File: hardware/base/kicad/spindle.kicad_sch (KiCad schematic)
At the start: 29 parts, among them J16 SPINDLE, Q5 AO3422, Q6 AO3422, U31 LM2904DR2G, U32 SN74AHCT1G125DBVR

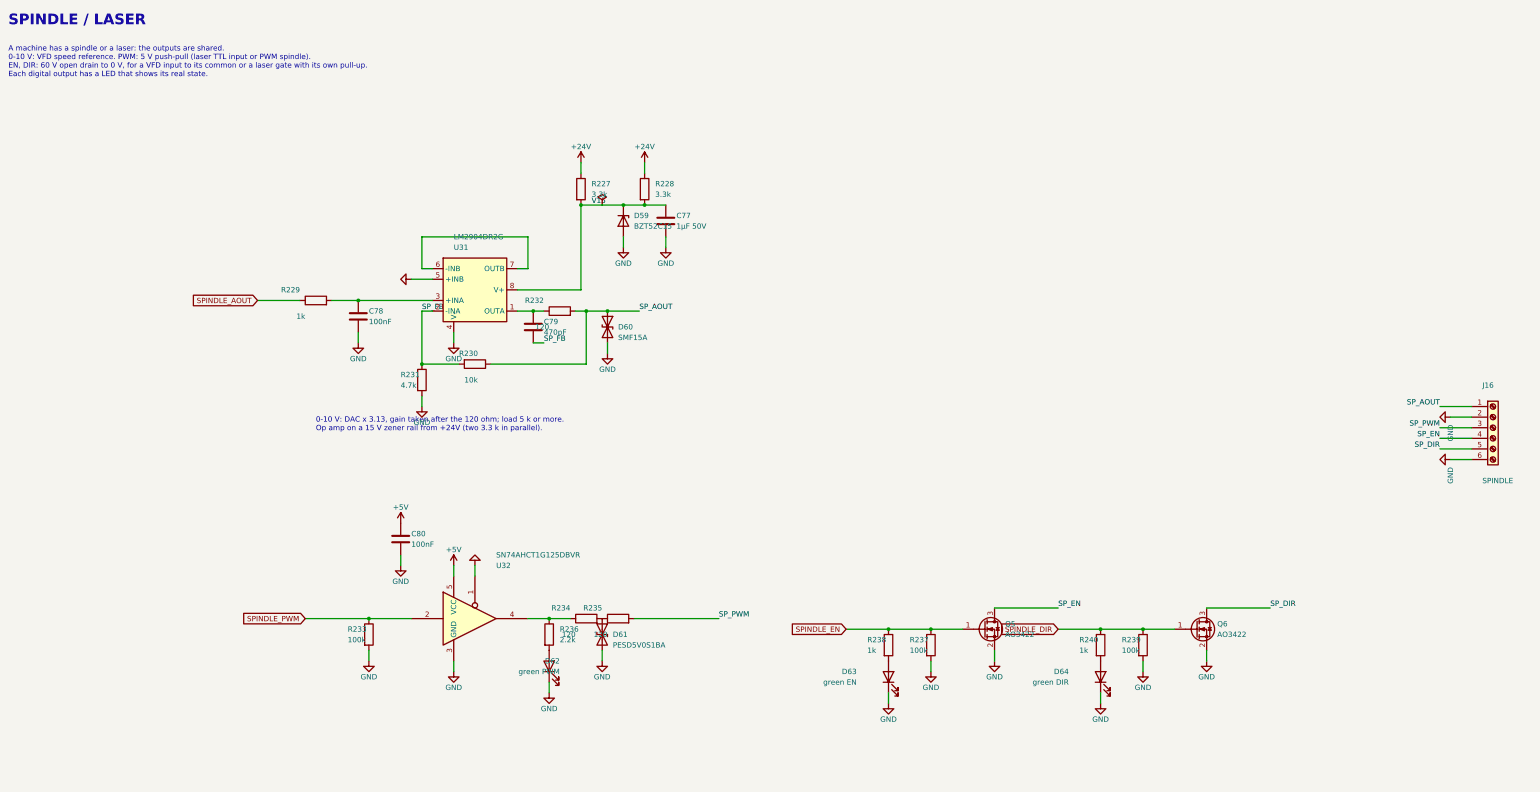
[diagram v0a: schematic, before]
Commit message: Harden the base board protections and unify its terminal blocks
- TVS (SMBJ33CA) on the spindle EN and DIR drains: a relay coil driven
  without a flyback diode no longer avalanches the FET.
- ESD (5 x TPD4E05U06) on every signal of the local bus header.
- A single terminal block type, KF2EDGR-3.81-4P, five times. Pinout rule:
  pole 1 withstands 24 V, pole 2 is 0 V, so the power plug damages
  nothing whichever header it lands in.
- Functional earth on pole 3 of the power terminal block, replacing the
  M3 earth lug.
- 100 k pull-down on the DAC node: the 0-10 V output stays at 0 V while
  the DAC pin is not configured (reset, bootloader).
- "24V OUT" LED on +24V_DRV and test points on the four rails.
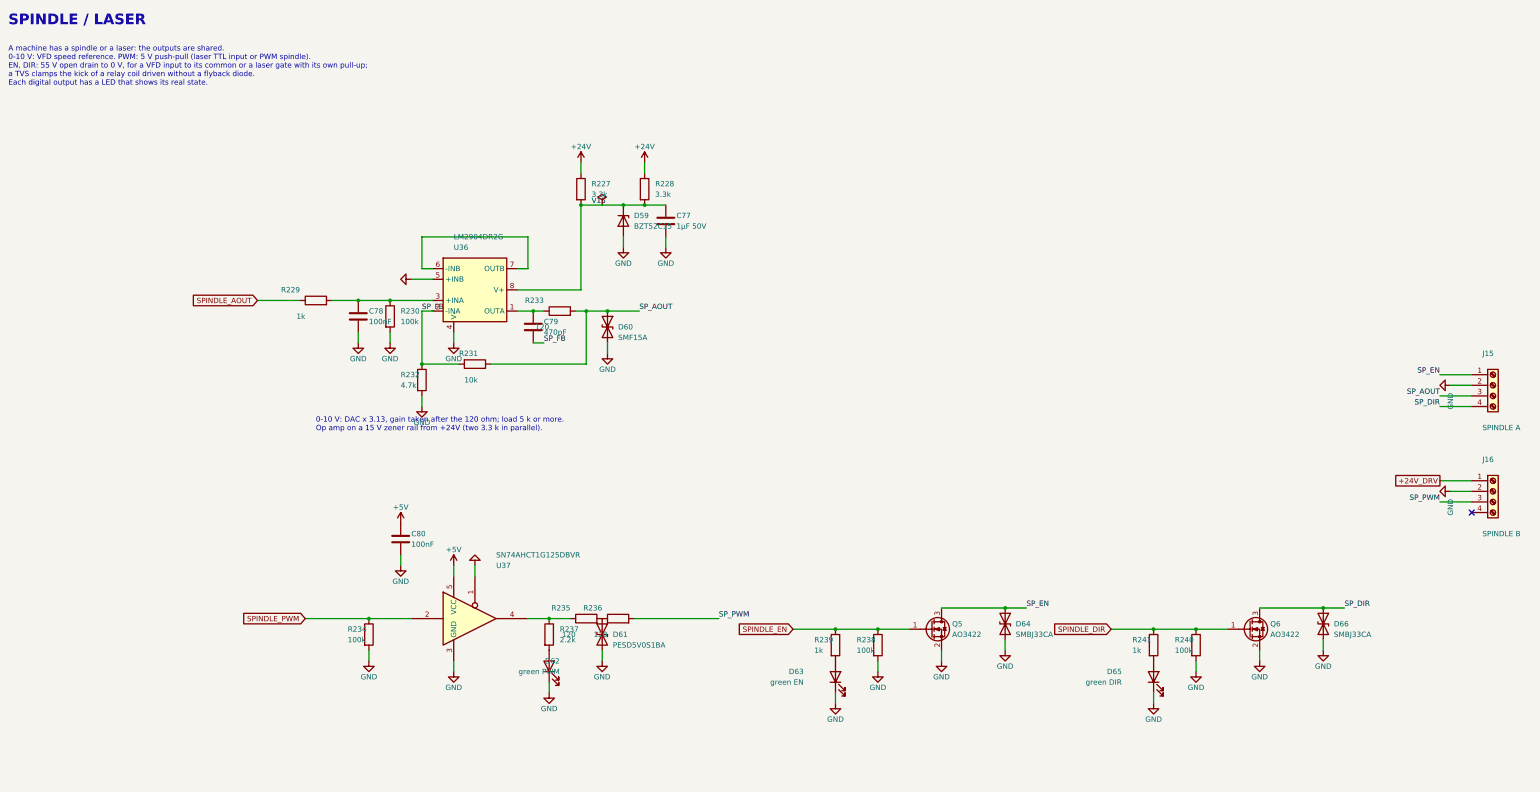
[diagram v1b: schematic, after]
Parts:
- removed U31: LM2904DR2G, Package_SO:SOIC-8_3.9x4.9mm_P1.27mm, symbol Bornier:OPAMP_DUAL
- removed U32: SN74AHCT1G125DBVR, Package_TO_SOT_SMD:SOT-23-5, symbol 74xGxx:74AHCT1G125
- added D65: green DIR, LED_SMD:LED_0603_1608Metric, symbol Device:LED
- added D66: SMBJ33CA, Diode_SMD:D_SMB, symbol Device:D_TVS
- added J15: SPINDLE A, Connector_Phoenix_MC:PhoenixContact_MC_1,5_4-G-3.81_1x04_P3.81mm_Horizontal, symbol Connector:Screw_Terminal_01x04
- added R241: 1k, Resistor_SMD:R_0402_1005Metric, symbol Device:R
- added U36: LM2904DR2G, Package_SO:SOIC-8_3.9x4.9mm_P1.27mm, symbol Bornier:OPAMP_DUAL
- added U37: SN74AHCT1G125DBVR, Package_TO_SOT_SMD:SOT-23-5, symbol 74xGxx:74AHCT1G125
- D64: value green DIR -> SMBJ33CA; footprint LED_SMD:LED_0603_1608Metric -> Diode_SMD:D_SMB; symbol Device:LED -> Device:D_TVS; LCSC C2289 -> C78420
- J16: value SPINDLE -> SPINDLE B; footprint Connector_Phoenix_MC:PhoenixContact_MC_1,5_6-G-3.81_1x06_P3.81mm_Horizontal -> Connector_Phoenix_MC:PhoenixContact_MC_1,5_4-G-3.81_1x04_P3.81mm_Horizontal; symbol Connector:Screw_Terminal_01x06 -> Connector:Screw_Terminal_01x04; LCSC C441186 -> C441184
- R230: value 10k -> 100k; LCSC C25744 -> C25741
- R231: value 4.7k -> 10k; LCSC C25900 -> C25744
- R232: value 120 -> 4.7k; footprint Resistor_SMD:R_0603_1608Metric -> Resistor_SMD:R_0402_1005Metric; LCSC C22787 -> C25900
- R233: value 100k -> 120; footprint Resistor_SMD:R_0402_1005Metric -> Resistor_SMD:R_0603_1608Metric; LCSC C25741 -> C22787
- R234: value 120 -> 100k; footprint Resistor_SMD:R_0603_1608Metric -> Resistor_SMD:R_0402_1005Metric; LCSC C22787 -> C25741
- R236: value 2.2k -> 120; footprint Resistor_SMD:R_0402_1005Metric -> Resistor_SMD:R_0603_1608Metric; LCSC C25879 -> C22787
- R237: value 100k -> 2.2k; LCSC C25741 -> C25879
- R238, R240: value 1k -> 100k; LCSC C11702 -> C25741
- R239: value 100k -> 1k; LCSC C25741 -> C11702
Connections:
- net +5V: now also U37.5 (VCC)
- net GND: now also D64.2 (A2), R230.2, R232.2, R234.2, R238.2, R240.2, D65.1 (K), D66.2 (A2), J15.2 (Pin_2), U36.4 (V-), U36.5 (+INB), U37.1, U37.3 (GND); no longer D64.1 (K), J16.6 (Pin_6), R231.2, R233.2, R237.2, R239.2
- net SPINDLE_DIR: now also R241.1; no longer R239.1
- net SPINDLE_EN: now also R239.1; no longer R237.1
- net SPINDLE_PWM: now also R234.1, U37.2; no longer R233.1
- net SP_AOUT: now also R231.1, R233.2, J15.3 (Pin_3); no longer J16.1 (Pin_1), R230.1, R232.2
- net SP_DIR: now also D66.1 (A1), J15.4 (Pin_4); no longer J16.5 (Pin_5)
- net SP_EN: now also D64.1 (A1), J15.1 (Pin_1); no longer J16.4 (Pin_4)
- net SP_FB: now also R231.2, R232.1, U36.2 (-INA); no longer R230.2, R231.1
- net SP_PWM: now also R236.2; no longer R235.2
- net V15: now also U36.8 (V+)
- net at D63.2 (A): now also R239.2; no longer R238.2
- net at C79.1: now also R233.1, U36.1 (OUTA); no longer R232.1
- net at R236.1: now also D61.1 (A1), R235.2; no longer R234.1
- net at D62.2 (A): now also R237.2; no longer R236.2
- net at C78.1, R229.2: now also R230.1, U36.3 (+INA)
- new net: D65.2 (A), R241.2
- new net: R235.1, R237.1, U37.4
- new net: U36.6 (-INB), U36.7 (OUTB)
- new net +24V_DRV: J16.1 (Pin_1)
- no-connect marks 0 -> 1
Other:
- note added: "A machine has a spindle or a laser: the outputs are shared. 0-10 V: VFD speed reference. PWM: 5 V push-pull (laser TTL input or PWM spindle). EN, DIR: 55 V open drain to 0 V, for a VFD input to its common or a laser gate with its own pull-up; a TVS clamps the kick of a relay coil driven without a flyback diode. Each digital output has a LED that shows its real state."
- note removed: "A machine has a spindle or a laser: the outputs are shared. 0-10 V: VFD speed reference. PWM: 5 V push-pull (laser TTL input or PWM spindle). EN, DIR: 60 V open drain to 0 V, for a VFD input to its common or a laser gate with its own pull-up. Each digital output has a LED that shows its real state."
- moved on the sheet: D63, Q5, Q6, R230, R231, R232, R233, R234, R235, R236, R237, R238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

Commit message: Accept a 12 V or 24 V supply on the base board (10.8 to 30 V)
- Supply nets renamed +VIN and +VIN_OUT (silkscreen VIN OUT).
- UVLO 200 k over 47 k // 100 k: start 8.47 V (9.48 V worst case),
  stop 7.79 V; fuse 3.5 A (12H1350C).
- 0-10 V: OPA2990 rail-to-rail op amp supplied by +VIN, SS8550 current
  limit across the 120 ohm; 10 V into 10 k from 10.9 V of supply.
- E-stop and probe inputs: 2 x 4.7 k in parallel, shunts 1 k and 4.7 k.
- Buck simulated from 7.8 to 30 V with the smallest slope compensation
  the datasheet allows: 79 deg, 11.6 dB minimum.
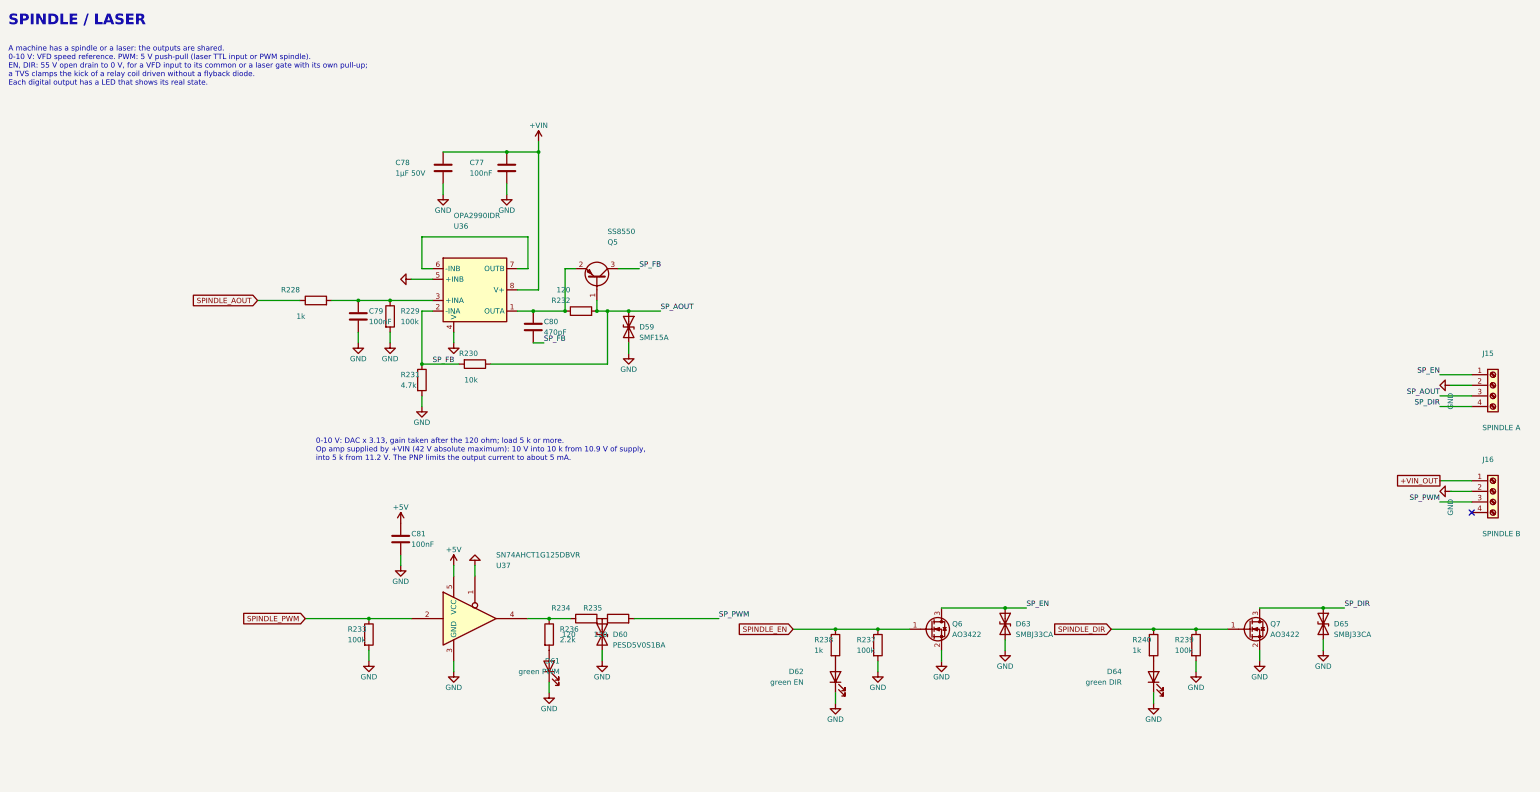
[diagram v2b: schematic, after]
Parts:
- removed D66: SMBJ33CA, Diode_SMD:D_SMB, symbol Device:D_TVS
- removed R227: 3.3k, Resistor_SMD:R_1206_3216Metric, symbol Device:R
- removed R241: 1k, Resistor_SMD:R_0402_1005Metric, symbol Device:R
- added C81: 100nF, Capacitor_SMD:C_0402_1005Metric, symbol Device:C
- added Q7: AO3422, Package_TO_SOT_SMD:SOT-23, symbol Transistor_FET:AO3400A
- C77: value 1µF 50V -> 100nF; footprint Capacitor_SMD:C_0603_1608Metric -> Capacitor_SMD:C_0402_1005Metric; LCSC C15849 -> C307331
- C78: value 100nF -> 1µF 50V; footprint Capacitor_SMD:C_0402_1005Metric -> Capacitor_SMD:C_0603_1608Metric; LCSC C307331 -> C15849
- C79: value 470pF -> 100nF; LCSC C1537 -> C307331
- C80: value 100nF -> 470pF; LCSC C307331 -> C1537
- D59: value BZT52C15 -> SMF15A; footprint Diode_SMD:D_SOD-123 -> Diode_SMD:D_SOD-123F; symbol Device:D_Zener -> Device:D_TVS; LCSC C2104 -> C123802
- D60: value SMF15A -> PESD5V0S1BA; footprint Diode_SMD:D_SOD-123F -> Diode_SMD:D_SOD-323; LCSC C123802 -> C19224
- D61: value PESD5V0S1BA -> green PWM; footprint Diode_SMD:D_SOD-323 -> LED_SMD:LED_0603_1608Metric; symbol Device:D_TVS -> Device:LED; LCSC C19224 -> C2289
- D62: value green PWM -> green EN
- D63: value green EN -> SMBJ33CA; footprint LED_SMD:LED_0603_1608Metric -> Diode_SMD:D_SMB; symbol Device:LED -> Device:D_TVS; LCSC C2289 -> C78420
- D64: value SMBJ33CA -> green DIR; footprint Diode_SMD:D_SMB -> LED_SMD:LED_0603_1608Metric; symbol Device:D_TVS -> Device:LED; LCSC C78420 -> C2289
- D65: value green DIR -> SMBJ33CA; footprint LED_SMD:LED_0603_1608Metric -> Diode_SMD:D_SMB; symbol Device:LED -> Device:D_TVS; LCSC C2289 -> C78420
- Q5: value AO3422 -> SS8550; symbol Transistor_FET:AO3400A -> Transistor_BJT:SS8550; LCSC C37130 -> C8542
- R228: value 3.3k -> 1k; footprint Resistor_SMD:R_1206_3216Metric -> Resistor_SMD:R_0402_1005Metric; LCSC C26032 -> C11702
- R229, R239: value 1k -> 100k; LCSC C11702 -> C25741
- R230: value 100k -> 10k; LCSC C25741 -> C25744
- R231: value 10k -> 4.7k; LCSC C25744 -> C25900
- R232: value 4.7k -> 120; footprint Resistor_SMD:R_0402_1005Metric -> Resistor_SMD:R_0603_1608Metric; LCSC C25900 -> C22787
- R233: value 120 -> 100k; footprint Resistor_SMD:R_0603_1608Metric -> Resistor_SMD:R_0402_1005Metric; LCSC C22787 -> C25741
- R234: value 100k -> 120; footprint Resistor_SMD:R_0402_1005Metric -> Resistor_SMD:R_0603_1608Metric; LCSC C25741 -> C22787
- R236: value 120 -> 2.2k; footprint Resistor_SMD:R_0603_1608Metric -> Resistor_SMD:R_0402_1005Metric; LCSC C22787 -> C25879
- R237: value 2.2k -> 100k; LCSC C25879 -> C25741
- R238, R240: value 100k -> 1k; LCSC C25741 -> C11702
- U36: value LM2904DR2G -> OPA2990IDR; LCSC C18229 -> C2058283
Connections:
- net +24V is gone; now on net SPINDLE_AOUT: R228.1
- net +5V: now also C81.1; no longer C80.1
- net GND: now also C79.2, D61.1 (K), D63.2 (A2), D64.1 (K), D65.2 (A2), R229.2, R231.2, R233.2, R237.2, R239.2, C81.2, Q7.2 (S); no longer C80.2, D61.2 (A2), D63.1 (K), D64.2 (A2), D65.1 (K), Q5.2 (S), R230.2, R232.2, R234.2, R238.2, R240.2
- net SPINDLE_AOUT: no longer R229.1
- net SPINDLE_DIR: now also R239.1, Q7.1 (G); no longer Q6.1 (G)
- net SPINDLE_EN: now also Q6.1 (G), R237.1; no longer Q5.1 (G), R239.1
- net SPINDLE_PWM: now also R233.1; no longer R234.1
- net SP_AOUT: now also D59.1 (A1), Q5.1 (B), R230.1, R232.2; no longer D60.1 (A1), R231.1, R233.2
- net SP_DIR: now also D65.1 (A1), Q7.3 (D); no longer Q6.3 (D)
- net SP_EN: now also D63.1 (A1), Q6.3 (D); no longer D64.1 (A1), Q5.3 (D)
- net SP_FB: now also C80.2, Q5.3 (C), R230.2, R231.1; no longer C79.2, R231.2, R232.1
- net SP_PWM: now also R235.2; no longer R236.2
- net at D62.2 (A): now also R238.2; no longer R237.2
- net +24V_DRV renamed +VIN_OUT
- net V15 renamed +VIN
- net +VIN: now also C78.1; no longer D59.1 (K), R228.2
- new net: D64.2 (A), R240.2
- new net: C80.1, Q5.2 (E), R232.1, U36.1 (OUTA)
- new net: R234.1, R236.1, U37.4
- new net: D61.2 (A), R236.2
- new net: D60.1 (A1), R234.2, R235.1
- new net: C79.1, R228.2, R229.1, U36.3 (+INA)
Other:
- note added: "0-10 V: DAC x 3.13, gain taken after the 120 ohm; load 5 k or more. Op amp supplied by +VIN (42 V absolute maximum): 10 V into 10 k from 10.9 V of supply, into 5 k from 11.2 V. The PNP limits the output current to about 5 mA."
- note removed: "0-10 V: DAC x 3.13, gain taken after the 120 ohm; load 5 k or more. Op amp on a 15 V zener rail from +24V (two 3.3 k in parallel)."
- moved on the sheet: C77, C78, C79, C80, D59, D60, D62, Q6, R228, R229, R230, R231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

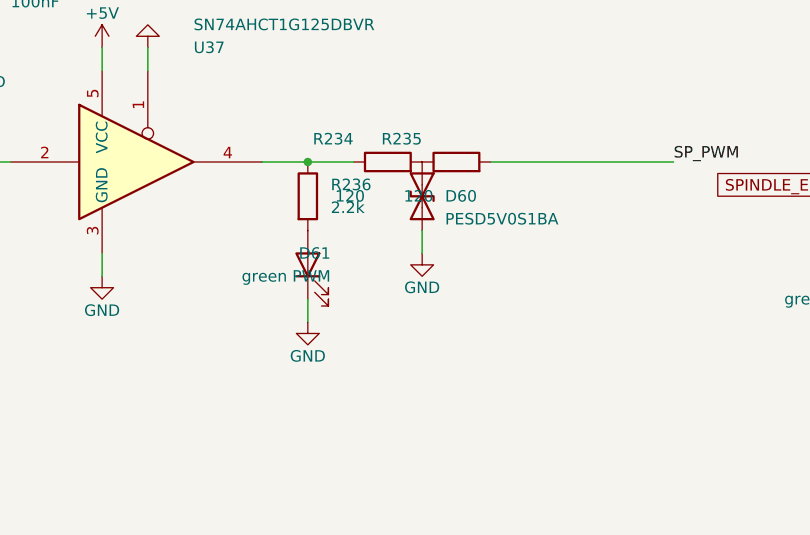
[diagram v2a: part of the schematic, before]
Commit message: Trim the base board BOM: 60 to 58 lines
- ESD of NRST and of the PWM output on one channel of the TPD4E05U06
  already used on the PHY lines, instead of a PESD5V0S1BA.
- SS56B instead of SS34 for the 5 V / USB OR-ing and the encoder
  supplies.
- One 100 uF 10 V X5R 1210 on the 5 V buck output instead of two 47 uF:
  about 55 uF at 5 V, inside the simulated 34-80 uF.
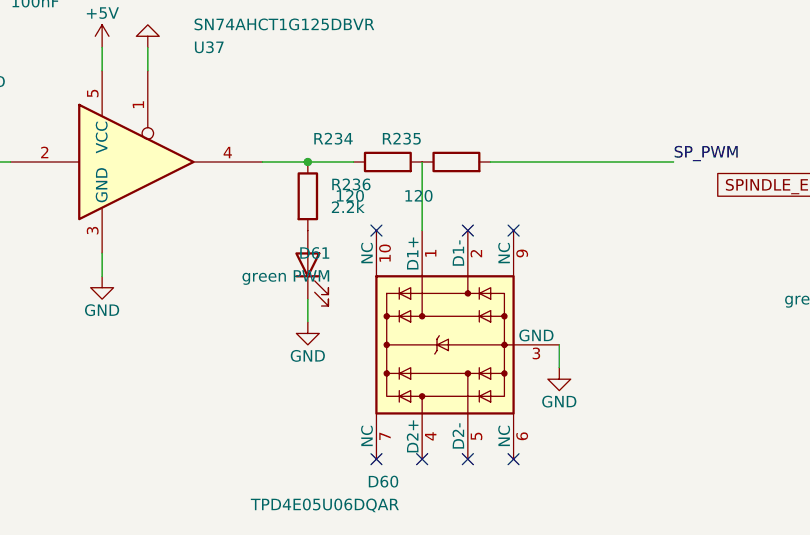
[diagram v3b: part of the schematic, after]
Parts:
- D60: value PESD5V0S1BA -> TPD4E05U06DQAR; footprint Diode_SMD:D_SOD-323 -> Package_SON:USON-10_2.5x1.0mm_P0.5mm; symbol Device:D_TVS -> Power_Protection:TPD4E05U06DQA; LCSC C19224 -> C138714
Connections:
- net GND: now also D60.3 (GND), D60.8 (GND); no longer D60.2 (A2)
- no-connect marks 1 -> 8

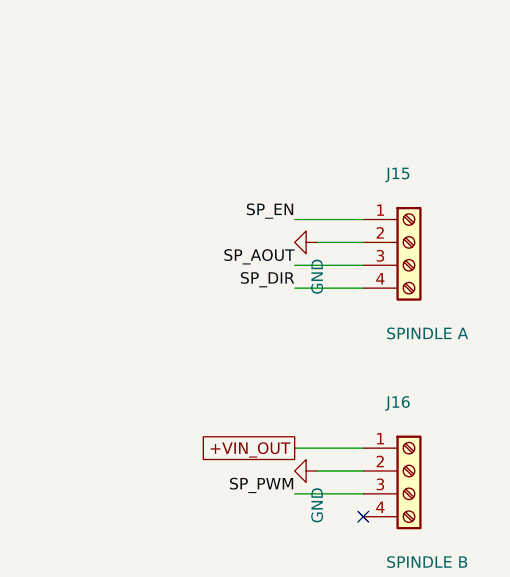
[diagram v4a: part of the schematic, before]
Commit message: Start the base board PCB: outline, profile rules, connectors on the edges
- pcb.py builds the board from the schematic: 72 x 150 mm, 4 layers,
  C-LOCK keyhole, M3 holes, connectors on both long edges; the other
  parts are parked beside the board until they are placed.
- base.kicad_dru: rules of the Phoenix UM-BASIC 72 profile (no part at
  the short edges on the top side, no through-hole lead on the rim the
  board rests on), proved by the DRC.
- Dual shielded RJ45 per axis (HC-WK88-H132-1X2-55B): port A for the
  drive, port B for the encoder. kicadgen draws multi-unit symbols, one
  unit per sheet; footprint and 3D model generated from the datasheet.
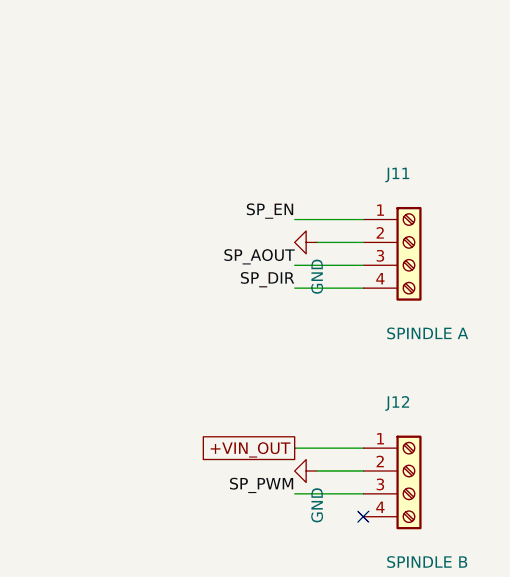
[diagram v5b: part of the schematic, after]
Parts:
- removed J15: SPINDLE A, Connector_Phoenix_MC:PhoenixContact_MC_1,5_4-G-3.81_1x04_P3.81mm_Horizontal, symbol Connector:Screw_Terminal_01x04
- removed J16: SPINDLE B, Connector_Phoenix_MC:PhoenixContact_MC_1,5_4-G-3.81_1x04_P3.81mm_Horizontal, symbol Connector:Screw_Terminal_01x04
- added J11: SPINDLE A, Connector_Phoenix_MC:PhoenixContact_MC_1,5_4-G-3.81_1x04_P3.81mm_Horizontal, symbol Connector:Screw_Terminal_01x04
- added J12: SPINDLE B, Connector_Phoenix_MC:PhoenixContact_MC_1,5_4-G-3.81_1x04_P3.81mm_Horizontal, symbol Connector:Screw_Terminal_01x04
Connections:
- net +VIN_OUT: now also J12.1 (Pin_1)
- net GND: now also J11.2 (Pin_2), J12.2 (Pin_2)
- net SP_AOUT: now also J11.3 (Pin_3)
- net SP_DIR: now also J11.4 (Pin_4)
- net SP_EN: now also J11.1 (Pin_1)
- net SP_PWM: now also J12.3 (Pin_3)
